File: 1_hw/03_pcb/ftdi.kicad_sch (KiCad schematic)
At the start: 34 parts, among them U13 93LC56BT-I_OT, U14 FT2232HL, Y2 12 MHz

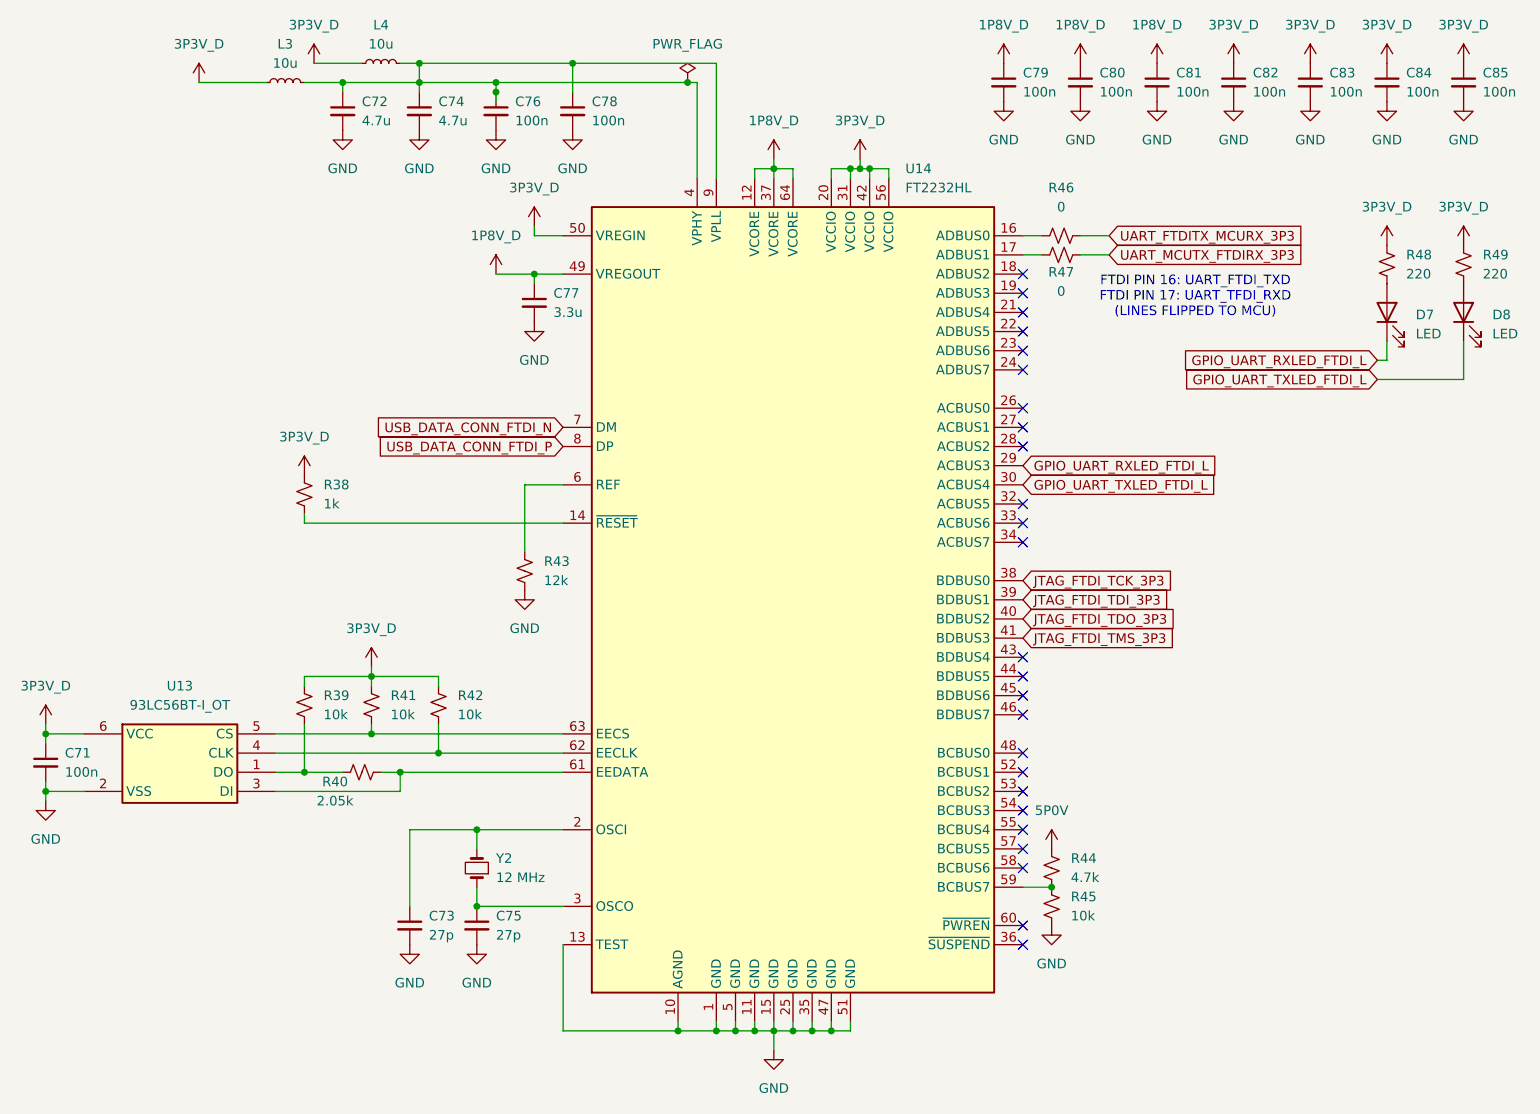
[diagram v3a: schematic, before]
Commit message: MINOR: Verified Footprints to Datasheets. Added Pull Ups on FPGA DONE/Config/SPI Chip Select Pins.
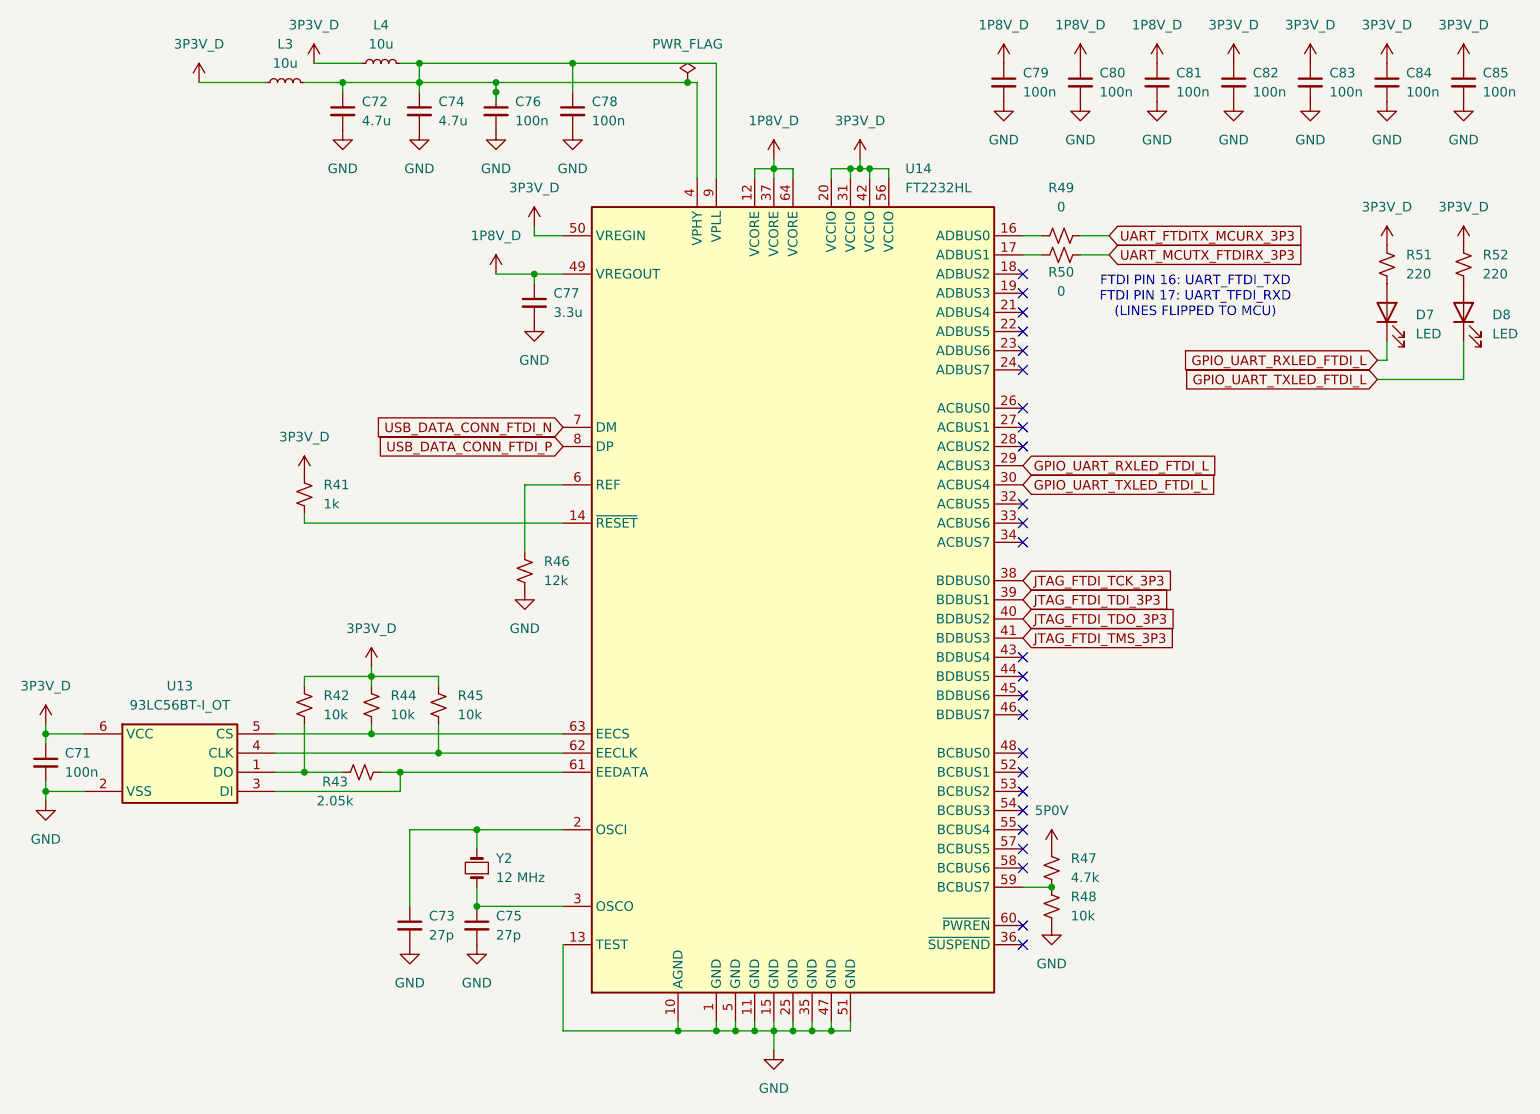
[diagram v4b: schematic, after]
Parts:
- renumbered R38 to R41, R39 to R42, R40 to R43, R41 to R44, R42 to R45, R43 to R46, R44 to R47, R45 to R48, R46 to R49, R47 to R50, R48 to R51, R49 to R52

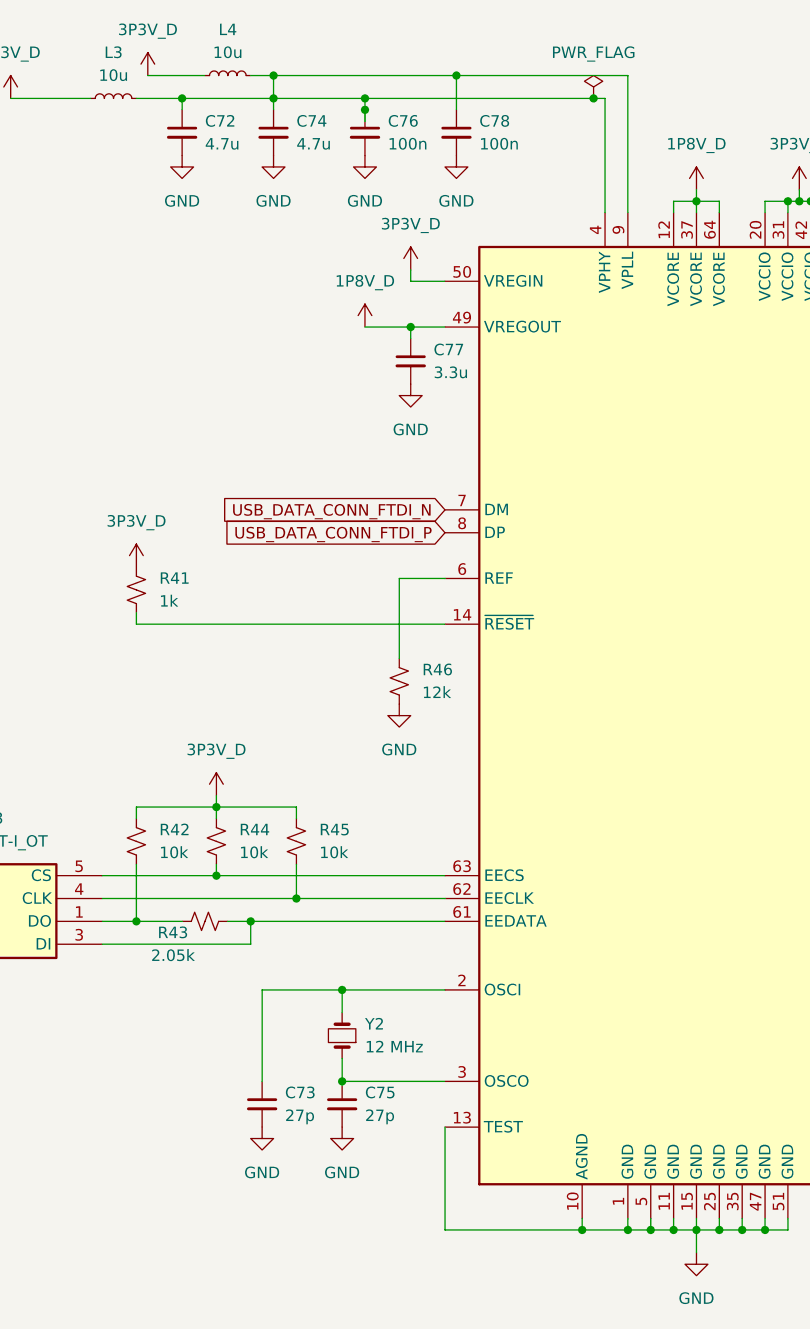
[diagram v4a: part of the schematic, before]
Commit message: FEAT: Initial board placement started.
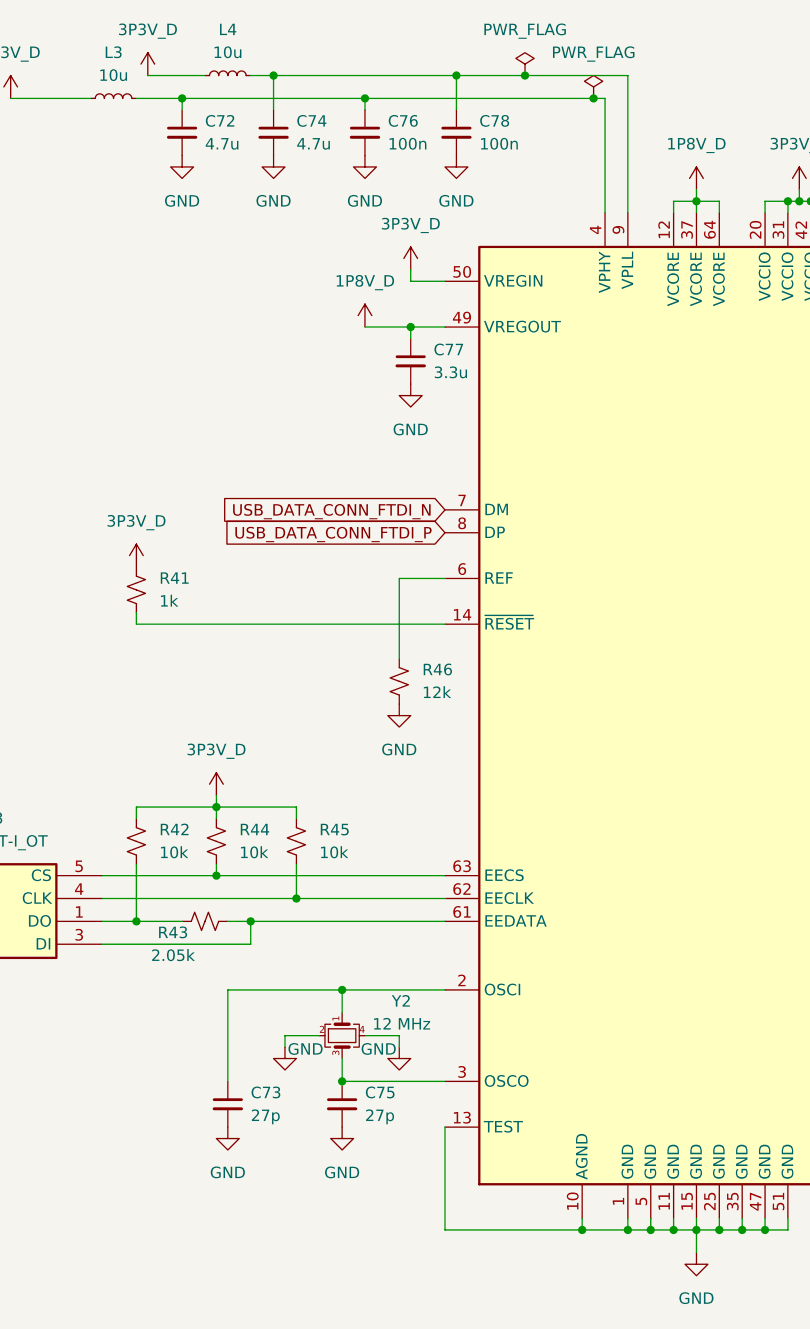
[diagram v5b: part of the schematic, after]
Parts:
- removed Y2: 12 MHz, Crystal:Crystal_SMD_3225-4Pin_3.2x2.5mm, symbol Device:Crystal_Small
- added Y2: 12 MHz, Crystal:Crystal_SMD_3225-4Pin_3.2x2.5mm, symbol Device:Crystal_GND24_Small
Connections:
- net GND: now also Y2.2, Y2.4
- net at C75.1, U14.3 (OSCO): now also Y2.3
- net at C73.1, U14.2 (OSCI): now also Y2.1
- net at C72.1, C76.1, L3.2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: no longer C74.1, C78.1, L4.2, U14.9 (VPLL)
- new net: C74.1, C78.1, L4.2, U14.9 (VPLL)
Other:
- moved on the sheet: C73
